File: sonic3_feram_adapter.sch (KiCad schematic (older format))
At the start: 2 parts, among them IC1 FM16W08-SG, P1 CONN_02X12

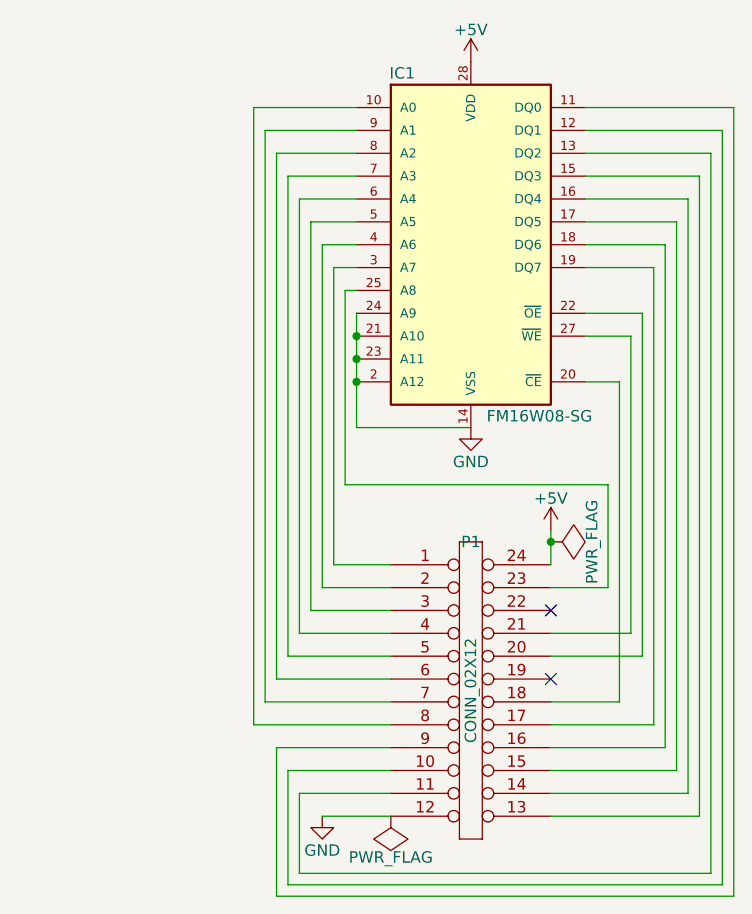
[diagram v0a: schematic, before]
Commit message: Added jumpers for bank selection
Since this board adapts an 8 KiB chip to work in the place of a 512 B
chip, it seems like it would be nice to allow the user to change which
block of 512 B is in use.  To allow this, I added solder bump jumpers to
the high address lines so they can be pulled to ground or 5 V.
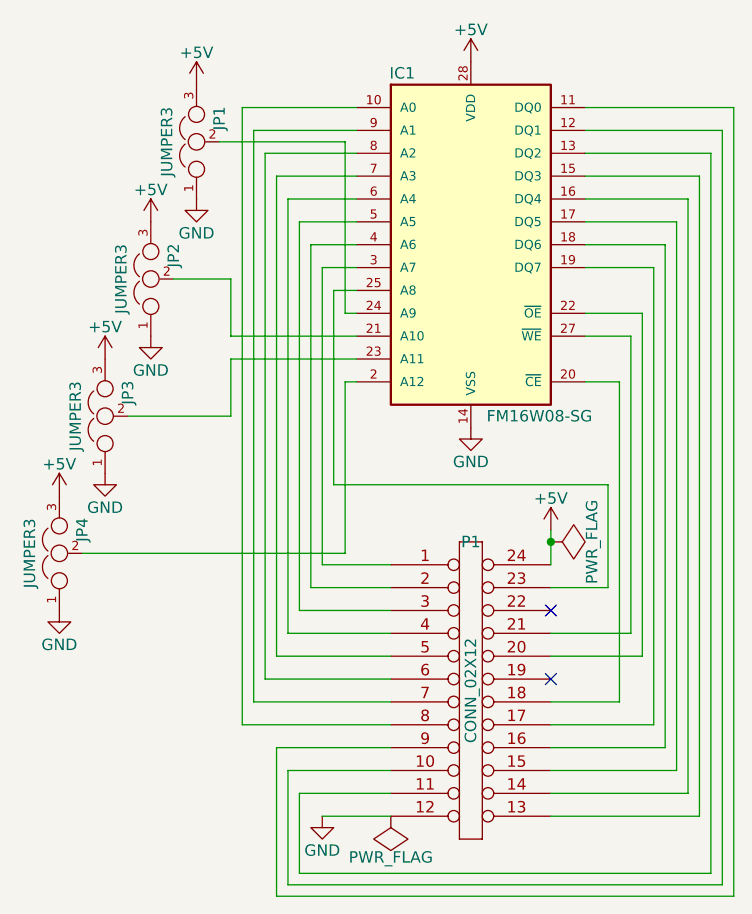
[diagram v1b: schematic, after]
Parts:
- added JP1, JP2, JP3, JP4: JUMPER3, jumper:SOLDER-JUMPER_2-WAY, symbol JUMPER3
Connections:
- net +5V: now also JP1.3, JP2.3, JP3.3, JP4.3
- net GND: now also JP1.1, JP2.1, JP3.1, JP4.1; no longer IC1.2 (A12), IC1.21 (A10), IC1.23 (A11), IC1.24 (A9)
- new net: IC1.2 (A12), JP4.2
- new net: IC1.21 (A10), JP2.2
- new net: IC1.23 (A11), JP3.2
- new net: IC1.24 (A9), JP1.2
